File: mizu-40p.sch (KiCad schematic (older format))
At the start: 5 parts

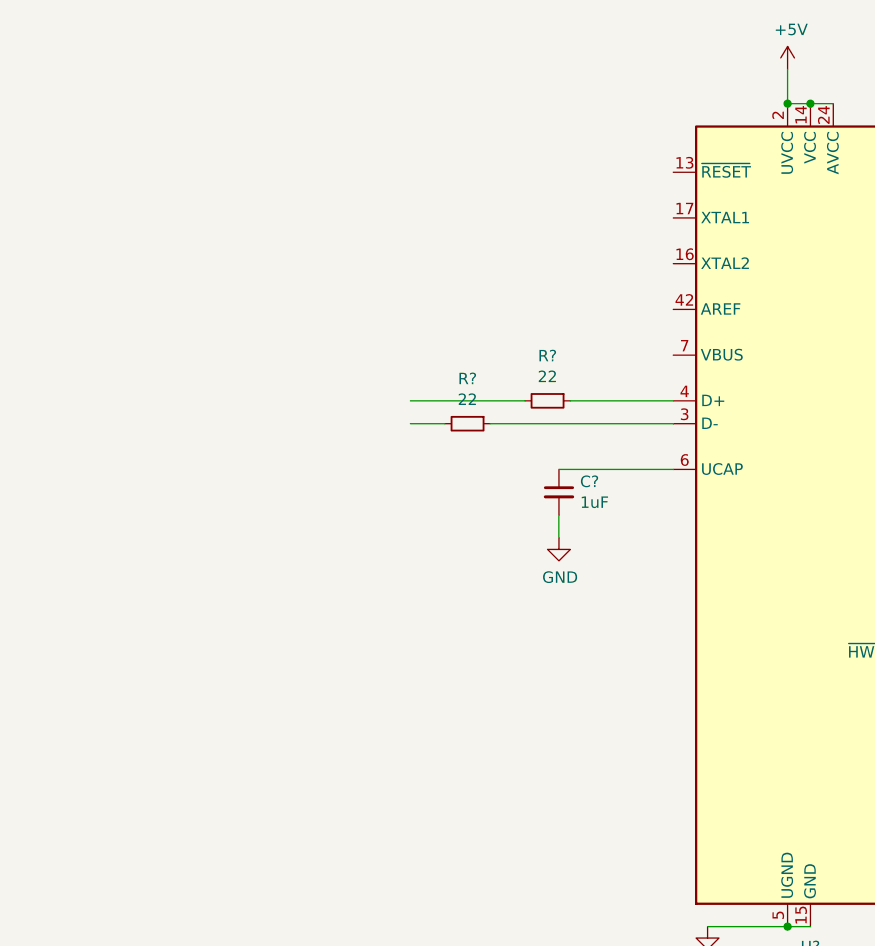
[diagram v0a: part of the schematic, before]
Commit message: Update MCU schematic
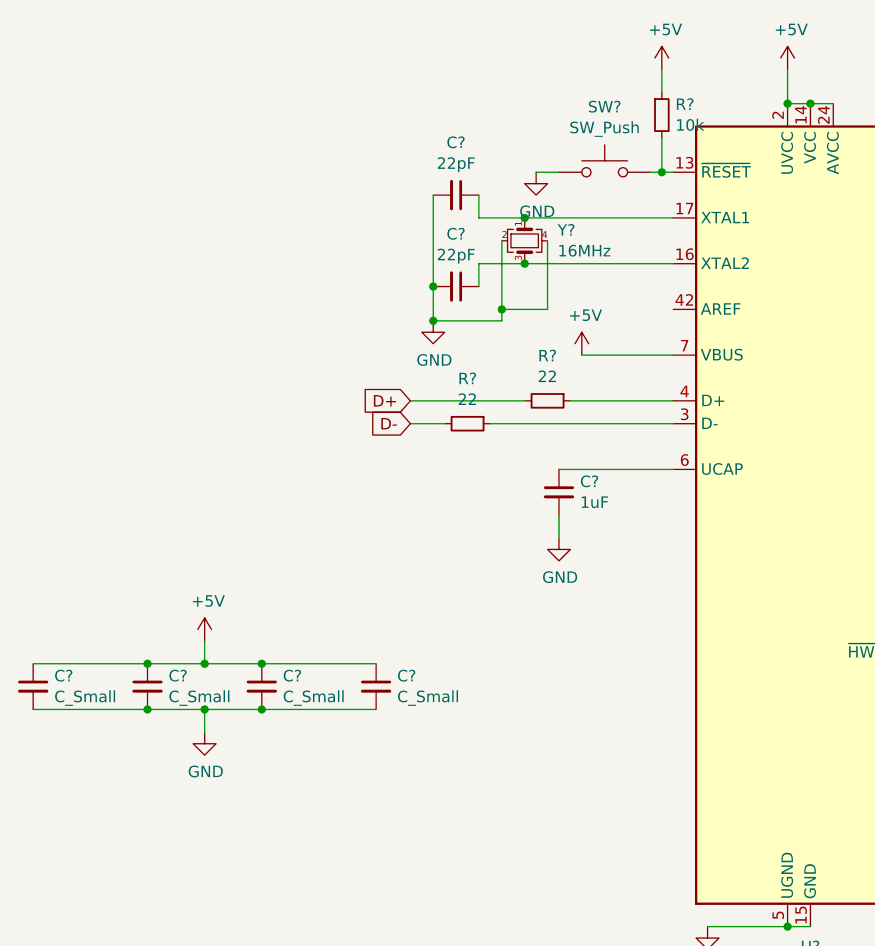
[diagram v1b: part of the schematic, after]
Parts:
- added C? (x4): C_Small, symbol Device:C_Small
- added C? (x2): 22pF, symbol Device:C_Small
- added R?: 10k, symbol Device:R_Small
- added SW?: SW_Push, symbol Switch:SW_Push
- added Y?: 16MHz, symbol Device:Crystal_GND24_Small
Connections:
- net labels added: D+, D-
- wire segments 13 -> 42
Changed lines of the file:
@@
 Wire Wire Line
 	4800 3900 4800 4000
+$Comp
+L Device:C_Small C?
+U 1 1 6242D745
+P 4000 4650
+F 0 "C?" H 4092 4696 50  0000 L CNN
+F 1 "C_Small" H 4092 4605 50  0000 L CNN
+F 2 "" H 4000 4650 50  0001 C CNN
+F 3 "~" H 4000 4650 50  0001 C CNN
+	1    4000 4650
+	1    0    0    -1
+$EndComp
+$Comp
+L Device:C_Small C?
+U 1 1 6242DE88
+P 3500 4650
+F 0 "C?" H 3592 4696 50  0000 L CNN
+F 1 "C_Small" H 3592 4605 50  0000 L CNN
+F 2 "" H 3500 4650 50  0001 C CNN
+F 3 "~" H 3500 4650 50  0001 C CNN
+	1    3500 4650
+	1    0    0    -1
+$EndComp
+$Comp
+L Device:C_Small C?
+U 1 1 6242E627
+P 3000 4650
+F 0 "C?" H 3092 4696 50  0000 L CNN
+F 1 "C_Small" H 3092 4605 50  0000 L CNN
+F 2 "" H 3000 4650 50  0001 C CNN
+F 3 "~" H 3000 4650 50  0001 C CNN
+	1    3000 4650
+	1    0    0    -1
+$EndComp
+$Comp
+L Device:C_Small C?
+U 1 1 6242F072
+P 2500 4650
+F 0 "C?" H 2592 4696 50  0000 L CNN
+F 1 "C_Small" H 2592 4605 50  0000 L CNN
+F 2 "" H 2500 4650 50  0001 C CNN
+F 3 "~" H 2500 4650 50  0001 C CNN
+	1    2500 4650
+	1    0    0    -1
+$EndComp
+Wire Wire Line
+	2500 4550 3000 4550
+Connection ~ 3000 4550
+Wire Wire Line
+	3000 4550 3250 4550
+Connection ~ 3500 4550
+Wire Wire Line
+	3500 4550 4000 4550
+Wire Wire Line
+	2500 4750 3000 4750
+Connection ~ 3000 4750
+Wire Wire Line
+	3000 4750 3250 4750
+Connection ~ 3500 4750
+Wire Wire Line
+	3500 4750 4000 4750
+Wire Wire Line
+	3250 4550 3250 4450
+Connection ~ 3250 4550
+Wire Wire Line
+	3250 4550 3500 4550
+Wire Wire Line
+	3250 4750 3250 4850
+Connection ~ 3250 4750
+Wire Wire Line
+	3250 4750 3500 4750
+$Comp
+L power:GND #PWR?
+U 1 1 62430518
+P 3250 4850
+F 0 "#PWR?" H 3250 4600 50  0001 C CNN
+F 1 "GND" H 3255 4677 50  0000 C CNN
+F 2 "" H 3250 4850 50  0001 C CNN
+F 3 "" H 3250 4850 50  0001 C CNN
+	1    3250 4850
+	1    0    0    -1
+$EndComp
+$Comp
+L power:+5V #PWR?
+U 1 1 62430967
+P 3250 4450
+F 0 "#PWR?" H 3250 4300 50  0001 C CNN
+F 1 "+5V" H 3265 4623 50  0000 C CNN
+F 2 "" H 3250 4450 50  0001 C CNN
+F 3 "" H 3250 4450 50  0001 C CNN
+	1    3250 4450
+	1    0    0    -1
+$EndComp
+$Comp
+L power:+5V #PWR?
+U 1 1 62430D9F
+P 4900 3200
+F 0 "#PWR?" H 4900 3050 50  0001 C CNN
+F 1 "+5V" H 4915 3373 50  0000 C CNN
+F 2 "" H 4900 3200 50  0001 C CNN
+F 3 "" H 4900 3200 50  0001 C CNN
+	1    4900 3200
+	1    0    0    -1
+$EndComp
+Wire Wire Line
+	4900 3200 5300 3200
+$Comp
+L Device:Crystal_GND24_Small Y?
+U 1 1 624344F3
+P 4650 2700
+F 0 "Y?" V 4604 2844 50  0000 L CNN
+F 1 "16MHz" V 4695 2844 50  0000 L CNN
+F 2 "" H 4650 2700 50  0001 C CNN
+F 3 "~" H 4650 2700 50  0001 C CNN
+	1    4650 2700
+	0    1    1    0
+$EndComp
+Wire Wire Line
+	5300 2800 4650 2800
+Wire Wire Line
+	4650 2600 5300 2600
+$Comp
+L Device:C_Small C?
+U 1 1 62435C6A
+P 4350 2500
+F 0 "C?" V 4121 2500 50  0000 C CNN
+F 1 "22pF" V 4212 2500 50  0000 C CNN
+F 2 "" H 4350 2500 50  0001 C CNN
+F 3 "~" H 4350 2500 50  0001 C CNN
+	1    4350 2500
+	0    1    1    0
+$EndComp
+$Comp
+L Device:C_Small C?
+U 1 1 624361F9
+P 4350 2900
+F 0 "C?" V 4121 2900 50  0000 C CNN
+F 1 "22pF" V 4212 2900 50  0000 C CNN
+F 2 "" H 4350 2900 50  0001 C CNN
+F 3 "~" H 4350 2900 50  0001 C CNN
+	1    4350 2900
+	0    1    1    0
+$EndComp
+Wire Wire Line
+	4650 2600 4450 2600
+Wire Wire Line
+	4450 2600 4450 2500
+Connection ~ 4650 2600
+Wire Wire Line
+	4250 2500 4250 2900
+Wire Wire Line
+	4650 2800 4450 2800
+Wire Wire Line
+	4450 2800 4450 2900
+Connection ~ 4650 2800
+Wire Wire Line
+	4550 2700 4550 3000
+Wire Wire Line
+	4550 3050 4250 3050
+Wire Wire Line
+	4750 2700 4750 3000
+Wire Wire Line
+	4750 3000 4550 3000
+Connection ~ 4550 3000
+Wire Wire Line
+	4550 3000 4550 3050
+Wire Wire Line
+	4250 2900 4250 3050
+Connection ~ 4250 2900
+$Comp
+L power:GND #PWR?
+U 1 1 62439709
+P 4250 3050
+F 0 "#PWR?" H 4250 2800 50  0001 C CNN
+F 1 "GND" H 4255 2877 50  0000 C CNN
+F 2 "" H 4250 3050 50  0001 C CNN
+F 3 "" H 4250 3050 50  0001 C CNN
+	1    4250 3050
+	1    0    0    -1
+$EndComp
+Connection ~ 4250 3050
+$Comp
+L power:GND #PWR?
+U 1 1 62439D83
+P 4700 2400
+F 0 "#PWR?" H 4700 2150 50  0001 C CNN
+F 1 "GND" H 4705 2227 50  0000 C CNN
+F 2 "" H 4700 2400 50  0001 C CNN
+F 3 "" H 4700 2400 50  0001 C CNN
+	1    4700 2400
+	1    0    0    -1
+$EndComp
+$Comp
+L Switch:SW_Push SW?
+U 1 1 6243A69C
+P 5000 2400
+F 0 "SW?" H 5000 2685 50  0000 C CNN
+F 1 "SW_Push" H 5000 2594 50  0000 C CNN
+F 2 "" H 5000 2600 50  0001 C CNN
+F 3 "~" H 5000 2600 50  0001 C CNN
+	1    5000 2400
+	1    0    0    -1
+$EndComp
+Wire Wire Line
+	4700 2400 4800 2400
+Wire Wire Line
+	5200 2400 5250 2400
+$Comp
+L Device:R_Small R?
+U 1 1 6243C0C8
+P 5250 2150
+F 0 "R?" H 5309 2196 50  0000 L CNN
+F 1 "10k" H 5309 2105 50  0000 L CNN
+F 2 "" H 5250 2150 50  0001 C CNN
+F 3 "~" H 5250 2150 50  0001 C CNN
+	1    5250 2150
+	1    0    0    -1
+$EndComp
+$Comp
+L power:+5V #PWR?
+U 1 1 6243C73E
+P 5250 1950
+F 0 "#PWR?" H 5250 1800 50  0001 C CNN
+F 1 "+5V" H 5265 2123 50  0000 C CNN
+F 2 "" H 5250 1950 50  0001 C CNN
+F 3 "" H 5250 1950 50  0001 C CNN
+	1    5250 1950
+	1    0    0    -1
+$EndComp
+Wire Wire Line
+	5250 2250 5250 2400
+Connection ~ 5250 2400
+Wire Wire Line
+	5250 2400 5300 2400
+Wire Wire Line
+	5250 1950 5250 2050
+Text GLabel 4150 3400 0    50   Input ~ 0
+D+
+Text GLabel 4150 3500 0    50   Input ~ 0
+D-
 $EndSCHEMATC

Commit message: Create switch matrix
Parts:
- added D? (x52): SOD-123, symbol Device:D_Small
- added MX? (x52): MX-NoLED, symbol MX_Alps_Hybrid:MX-NoLED
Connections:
- net GND: no longer C?.2, C?.2, C?.2, C?.2
- new net: C?.2, C?.2, C?.2, C?.2
- new net: D?.2 (A), MX?.2 (ROW) (x52)
- new net COL0: MX?.1 (COL), MX?.1 (COL), MX?.1 (COL), MX?.1 (COL), MX?.1 (COL)
- new net COL1: MX?.1 (COL), MX?.1 (COL), MX?.1 (COL), MX?.1 (COL), MX?.1 (COL)
- new net COL10: MX?.1 (COL), MX?.1 (COL), MX?.1 (COL), MX?.1 (COL)
- new net COL11: MX?.1 (COL), MX?.1 (COL), MX?.1 (COL), MX?.1 (COL)
- new net COL2: MX?.1 (COL), MX?.1 (COL), MX?.1 (COL), MX?.1 (COL), MX?.1 (COL)
- new net COL3: MX?.1 (COL), MX?.1 (COL), MX?.1 (COL), MX?.1 (COL), MX?.1 (COL)
- new net COL4: MX?.1 (COL), MX?.1 (COL), MX?.1 (COL), MX?.1 (COL), MX?.1 (COL)
- new net COL5: MX?.1 (COL), MX?.1 (COL), MX?.1 (COL), MX?.1 (COL)
- new net COL6: MX?.1 (COL), MX?.1 (COL), MX?.1 (COL)
- new net COL7: MX?.1 (COL), MX?.1 (COL), MX?.1 (COL), MX?.1 (COL)
- new net COL8: MX?.1 (COL), MX?.1 (COL), MX?.1 (COL), MX?.1 (COL)
- new net COL9: MX?.1 (COL), MX?.1 (COL), MX?.1 (COL), MX?.1 (COL)
- new net ROW0: D?.1 (K), D?.1 (K), D?.1 (K), D?.1 (K), D?.1 (K)
- new net ROW1: D?.1 (K), D?.1 (K), D?.1 (K), D?.1 (K), D?.1 (K), D?.1 (K), D?.1 (K), D?.1 (K), D?.1 (K), D?.1 (K), D?.1 (K), D?.1 (K)
- new net ROW2: D?.1 (K), D?.1 (K), D?.1 (K), D?.1 (K), D?.1 (K), D?.1 (K), D?.1 (K), D?.1 (K), D?.1 (K), D?.1 (K), D?.1 (K), D?.1 (K)
- new net ROW3: D?.1 (K), D?.1 (K), D?.1 (K), D?.1 (K), D?.1 (K), D?.1 (K), D?.1 (K), D?.1 (K), D?.1 (K), D?.1 (K), D?.1 (K), D?.1 (K)
- new net ROW4: D?.1 (K), D?.1 (K), D?.1 (K), D?.1 (K), D?.1 (K), D?.1 (K), D?.1 (K), D?.1 (K), D?.1 (K), D?.1 (K), D?.1 (K)
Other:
- moved on the sheet: C?, R?, SW?, U?, Y?

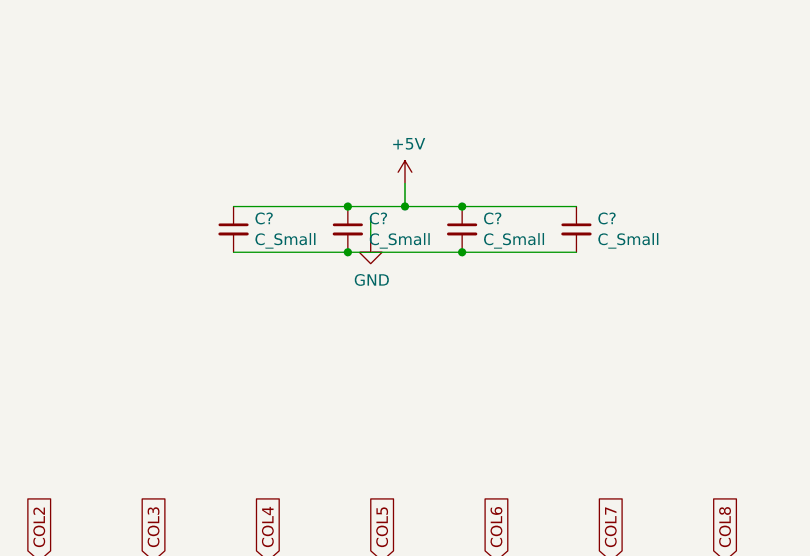
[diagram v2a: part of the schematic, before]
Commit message: Update improper GND connection for decoupling capacitors
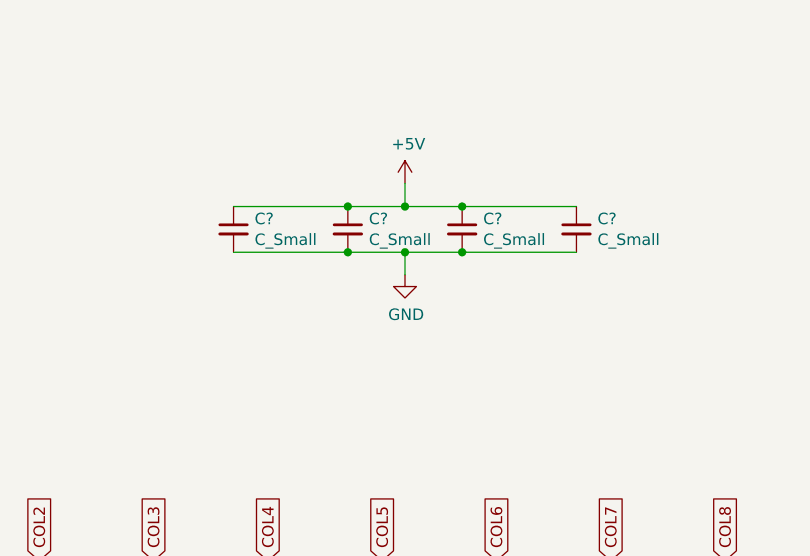
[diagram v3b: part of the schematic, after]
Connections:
- net GND: now also C?.2, C?.2, C?.2, C?.2
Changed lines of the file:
@@
-$Comp
-L Device:C_Small C?
-U 1 1 6242E627
-P 4100 1600
-F 0 "C?" H 4192 1646 50  0000 L CNN
-F 1 "C_Small" H 4192 1555 50  0000 L CNN
-F 2 "" H 4100 1600 50  0001 C CNN
-F 3 "~" H 4100 1600 50  0001 C CNN
-	1    4100 1600
-	1    0    0    -1
-$EndComp
 $Comp
 L Device:C_Small C?
@@
 $EndComp
 Wire Wire Line
-	3600 1500 4100 1500
-Connection ~ 4100 1500
-Wire Wire Line
-	4100 1500 4350 1500
-Wire Wire Line
 	3600 1700 4100 1700
-Connection ~ 4100 1700
 Wire Wire Line
 	4350 1500 4350 1400
 Connection ~ 4350 1500
-Wire Wire Line
-	4200 1550 4200 1650
-$Comp
-L power:GND #PWR?
-U 1 1 62430518
-P 4200 1650
-F 0 "#PWR?" H 4200 1400 50  0001 C CNN
-F 1 "GND" H 4205 1477 50  0000 C CNN
-F 2 "" H 4200 1650 50  0001 C CNN
-F 3 "" H 4200 1650 50  0001 C CNN
-	1    4200 1650
-	1    0    0    -1
-$EndComp
 $Comp
 L power:+5V #PWR?
@@
 Wire Wire Line
 	4350 1500 4600 1500
-Wire Wire Line
-	4100 1700 4600 1700
 Connection ~ 4600 1500
 Wire Wire Line
 	4600 1500 5100 1500
-Connection ~ 4600 1700
 Wire Wire Line
 	4600 1700 5100 1700
@@
 Text GLabel 7250 3050 1    50   Input ~ 0
 COL11
+Connection ~ 4600 1700
+Connection ~ 4100 1700
+Connection ~ 4100 1500
+Wire Wire Line
+	4100 1500 4350 1500
+Wire Wire Line
+	3600 1500 4100 1500
+Wire Wire Line
+	4100 1700 4350 1700
+$Comp
+L power:GND #PWR?
+U 1 1 62430518
+P 4350 1800
+F 0 "#PWR?" H 4350 1550 50  0001 C CNN
+F 1 "GND" H 4355 1627 50  0000 C CNN
+F 2 "" H 4350 1800 50  0001 C CNN
+F 3 "" H 4350 1800 50  0001 C CNN
+	1    4350 1800
+	1    0    0    -1
+$EndComp
+$Comp
+L Device:C_Small C?
+U 1 1 6242E627
+P 4100 1600
+F 0 "C?" H 4192 1646 50  0000 L CNN
+F 1 "C_Small" H 4192 1555 50  0000 L CNN
+F 2 "" H 4100 1600 50  0001 C CNN
+F 3 "~" H 4100 1600 50  0001 C CNN
+	1    4100 1600
+	1    0    0    -1
+$EndComp
+Wire Wire Line
+	4350 1800 4350 1700
+Connection ~ 4350 1700
+Wire Wire Line
+	4350 1700 4600 1700
 $EndSCHEMATC

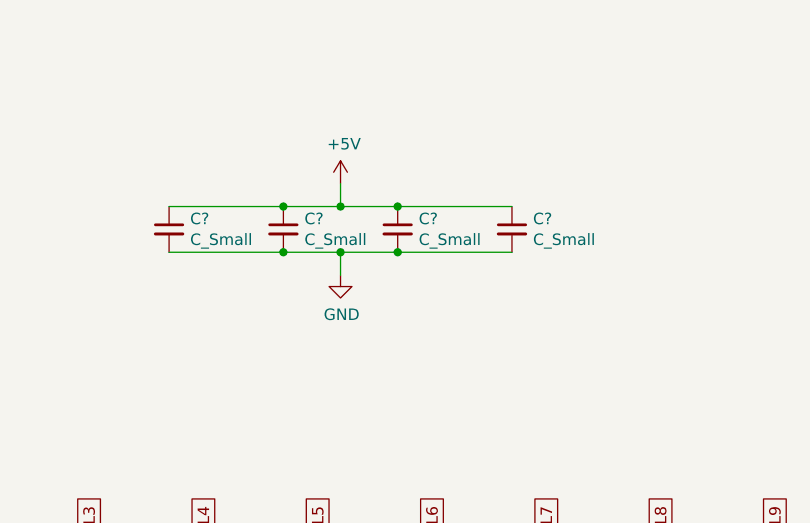
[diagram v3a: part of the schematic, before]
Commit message: Update capacitance of decoupling capacitors
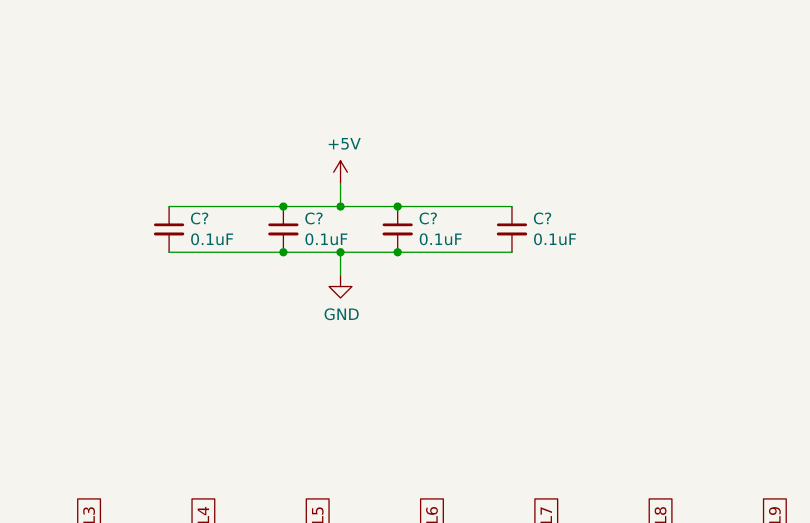
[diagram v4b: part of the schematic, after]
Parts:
- C? (x4): value C_Small -> 0.1uF
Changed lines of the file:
@@
 P 5100 1600
 F 0 "C?" H 5192 1646 50  0000 L CNN
-F 1 "C_Small" H 5192 1555 50  0000 L CNN
+F 1 "0.1uF" H 5192 1555 50  0000 L CNN
 F 2 "" H 5100 1600 50  0001 C CNN
 F 3 "~" H 5100 1600 50  0001 C CNN
@@
 P 4600 1600
 F 0 "C?" H 4692 1646 50  0000 L CNN
-F 1 "C_Small" H 4692 1555 50  0000 L CNN
+F 1 "0.1uF" H 4692 1555 50  0000 L CNN
 F 2 "" H 4600 1600 50  0001 C CNN
 F 3 "~" H 4600 1600 50  0001 C CNN
@@
 P 3600 1600
 F 0 "C?" H 3692 1646 50  0000 L CNN
-F 1 "C_Small" H 3692 1555 50  0000 L CNN
+F 1 "0.1uF" H 3692 1555 50  0000 L CNN
 F 2 "" H 3600 1600 50  0001 C CNN
 F 3 "~" H 3600 1600 50  0001 C CNN
@@
 P 4100 1600
 F 0 "C?" H 4192 1646 50  0000 L CNN
-F 1 "C_Small" H 4192 1555 50  0000 L CNN
+F 1 "0.1uF" H 4192 1555 50  0000 L CNN
 F 2 "" H 4100 1600 50  0001 C CNN
 F 3 "~" H 4100 1600 50  0001 C CNN

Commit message: Change layout
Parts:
- removed D? (x45): SOD-123, symbol Device:D_Small
- removed MX? (x45): MX-NoLED, symbol MX_Alps_Hybrid:MX-NoLED
- added D1, D10, D11, D12, D13, D14, D15, D16, D17, D18, D19, D2, D20, D21, D22, D23, D24, D25, D26, D27, D28, D29, D3, D30, D31, D32, D33, D34, D35, D36, D37, D38, D39, D4, D40, D41, D42, D43, D44, D45, D46, D47, D48, D49, D5, D50, D6, D7, D8, D9: SOD-123, Diode_SMD:D_SOD-123, symbol Device:D_Small
- added MX1, MX10, MX11, MX12, MX13, MX14, MX15, MX16, MX17, MX18, MX19, MX2, MX20, MX21, MX22, MX23, MX24, MX25, MX26, MX27, MX28, MX29, MX3, MX30, MX31, MX32, MX33, MX34, MX35, MX36, MX37, MX38, MX39, MX4, MX40, MX41, MX42, MX43, MX44, MX45, MX46, MX47, MX48, MX49, MX5, MX50, MX6, MX7, MX8, MX9: MX-NoLED, MX_Alps_Hybrid:MX-1U-NoLED, symbol MX_Alps_Hybrid:MX-NoLED
- C1, C2, C3, C4, C5, C6, C7: renamed from C?; footprint (none) -> Capacitor_SMD:C_0805_2012Metric
- D51, D52, D53, D54, D55, D56, D57: renamed from D?; footprint (none) -> Diode_SMD:D_SOD-123
- MX51, MX52, MX53, MX54, MX55, MX56, MX57: renamed from MX?; footprint (none) -> MX_Alps_Hybrid:MX-1U-NoLED
- R1, R2, R3, R4: renamed from R?; footprint (none) -> Resistor_SMD:R_0805_2012Metric
- SW1: renamed from SW?; footprint (none) -> random-keyboard-parts:SKQG-1155865
- gave numbers to parts that had none: 2
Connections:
- net COL0: now also MX1.1 (COL), MX13.1 (COL), MX25.1 (COL), MX37.1 (COL), MX49.1 (COL); no longer MX51.1 (COL)
- net COL1: now also MX14.1 (COL), MX2.1 (COL), MX26.1 (COL), MX38.1 (COL), MX50.1 (COL)
- net COL10: now also MX11.1 (COL), MX23.1 (COL), MX35.1 (COL), MX47.1 (COL)
- net COL11: now also MX12.1 (COL), MX24.1 (COL), MX36.1 (COL), MX48.1 (COL)
- net COL2: now also MX51.1 (COL), MX15.1 (COL), MX27.1 (COL), MX3.1 (COL), MX39.1 (COL)
- net COL3: now also MX16.1 (COL), MX28.1 (COL), MX4.1 (COL), MX40.1 (COL); no longer MX52.1 (COL)
- net COL4: now also MX17.1 (COL), MX29.1 (COL), MX41.1 (COL), MX5.1 (COL); no longer MX53.1 (COL)
- net COL5: now also MX52.1 (COL), MX18.1 (COL), MX30.1 (COL), MX42.1 (COL), MX6.1 (COL)
- net COL6: now also MX53.1 (COL), MX19.1 (COL), MX31.1 (COL), MX43.1 (COL), MX7.1 (COL)
- net COL7: now also MX20.1 (COL), MX32.1 (COL), MX44.1 (COL), MX8.1 (COL)
- net COL8: now also MX21.1 (COL), MX33.1 (COL), MX45.1 (COL), MX9.1 (COL)
- net COL9: now also MX10.1 (COL), MX22.1 (COL), MX34.1 (COL), MX46.1 (COL)
- net ROW0: now also D1.1 (K), D10.1 (K), D11.1 (K), D12.1 (K), D2.1 (K), D3.1 (K), D4.1 (K), D5.1 (K), D6.1 (K), D7.1 (K), D8.1 (K), D9.1 (K)
- net ROW1: now also D13.1 (K), D14.1 (K), D15.1 (K), D16.1 (K), D17.1 (K), D18.1 (K), D19.1 (K), D20.1 (K), D21.1 (K), D22.1 (K), D23.1 (K), D24.1 (K)
- net ROW2: now also D25.1 (K), D26.1 (K), D27.1 (K), D28.1 (K), D29.1 (K), D30.1 (K), D31.1 (K), D32.1 (K), D33.1 (K), D34.1 (K), D35.1 (K), D36.1 (K)
- net ROW3: now also D37.1 (K), D38.1 (K), D39.1 (K), D40.1 (K), D41.1 (K), D42.1 (K), D43.1 (K), D44.1 (K), D45.1 (K), D46.1 (K), D47.1 (K), D48.1 (K)
- net ROW4: now also D49.1 (K), D50.1 (K)
- new net: D50.2 (A), MX50.2 (ROW)
- new net: D49.2 (A), MX49.2 (ROW)
- new net: D39.2 (A), MX39.2 (ROW)
- new net: D40.2 (A), MX40.2 (ROW)
- new net: D41.2 (A), MX41.2 (ROW)
- new net: D42.2 (A), MX42.2 (ROW)
- new net: D43.2 (A), MX43.2 (ROW)
- new net: D44.2 (A), MX44.2 (ROW)
- new net: D45.2 (A), MX45.2 (ROW)
- new net: D46.2 (A), MX46.2 (ROW)
- new net: D47.2 (A), MX47.2 (ROW)
- new net: D48.2 (A), MX48.2 (ROW)
- new net: D38.2 (A), MX38.2 (ROW)
- new net: D37.2 (A), MX37.2 (ROW)
- new net: D27.2 (A), MX27.2 (ROW)
- new net: D28.2 (A), MX28.2 (ROW)
- new net: D29.2 (A), MX29.2 (ROW)
- new net: D30.2 (A), MX30.2 (ROW)
- new net: D31.2 (A), MX31.2 (ROW)
- new net: D32.2 (A), MX32.2 (ROW)
- new net: D33.2 (A), MX33.2 (ROW)
- new net: D34.2 (A), MX34.2 (ROW)
- new net: D35.2 (A), MX35.2 (ROW)
- new net: D36.2 (A), MX36.2 (ROW)
- new net: D26.2 (A), MX26.2 (ROW)
- new net: D25.2 (A), MX25.2 (ROW)
- new net: D15.2 (A), MX15.2 (ROW)
- new net: D16.2 (A), MX16.2 (ROW)
- new net: D17.2 (A), MX17.2 (ROW)
- new net: D18.2 (A), MX18.2 (ROW)
- new net: D19.2 (A), MX19.2 (ROW)
- new net: D20.2 (A), MX20.2 (ROW)
- new net: D21.2 (A), MX21.2 (ROW)
- new net: D22.2 (A), MX22.2 (ROW)
- new net: D23.2 (A), MX23.2 (ROW)
- new net: D24.2 (A), MX24.2 (ROW)
- new net: D14.2 (A), MX14.2 (ROW)
- new net: D13.2 (A), MX13.2 (ROW)
- new net: D3.2 (A), MX3.2 (ROW)
- new net: D4.2 (A), MX4.2 (ROW)
- new net: D5.2 (A), MX5.2 (ROW)
- new net: D6.2 (A), MX6.2 (ROW)
- new net: D7.2 (A), MX7.2 (ROW)
- new net: D8.2 (A), MX8.2 (ROW)
- new net: D9.2 (A), MX9.2 (ROW)
- new net: D10.2 (A), MX10.2 (ROW)
- new net: D11.2 (A), MX11.2 (ROW)
- new net: D12.2 (A), MX12.2 (ROW)
- new net: D2.2 (A), MX2.2 (ROW)
- new net: D1.2 (A), MX1.2 (ROW)
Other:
- moved on the sheet: C1, C2, C3, C4, C5, C6, C7, D51, D52, D53, D54, D55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
